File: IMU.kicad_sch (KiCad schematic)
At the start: 1 part, among them U1 RASPBERRY_PI_ZERO_2_W

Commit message: IMU schematic made
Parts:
- added J1: Conn_01x07_Socket, symbol Connector:Conn_01x07_Socket
- added J2: LCD Display, symbol Connector:Conn_01x04_Socket
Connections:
- net IMU_VCC: now reaches U1.1 (3V3_1)
- net IMU_VCC: now also J1.1 (Pin_1)
- net LCD_VCC: now reaches U1.17 (3V3_17)
- net LCD_VCC: now also J2.3 (Pin_3)
- net LCD_SDA: now reaches U1.24 (GPIO8/SPI_~{CE0})
- net LCD_SDA: now also J2.2 (Pin_2)
- net LCD_SCL: now reaches U1.26 (GPIO7/SPI_~{CE1})
- net LCD_SCL: now also J2.1 (Pin_1)
- net IMU_SCL: now reaches U1.29 (GPIO5)
- net IMU_SCL: now also J1.3 (Pin_3)
- net IMU_SDA: now reaches U1.31 (GPIO6)
- net IMU_SDA: now also J1.4 (Pin_4)
- net IMU_GND: now reaches U1.6 (GND_6)
- net IMU_GND: now also J1.2 (Pin_2)
- net LCD_GND: now reaches U1.9 (GND_9)
- net LCD_GND: now also J2.4 (Pin_4)
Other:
- note added: "IMU PINS: 1 - VCC 2 - GND 3 - SCL 4 - SDA 5 - XDA 6 - XCL 7 - INT"
- note added: "LCD PINS: 1 - SDA 2 - SCL 3 - VCC 4 - GND"
- moved on the sheet: U1

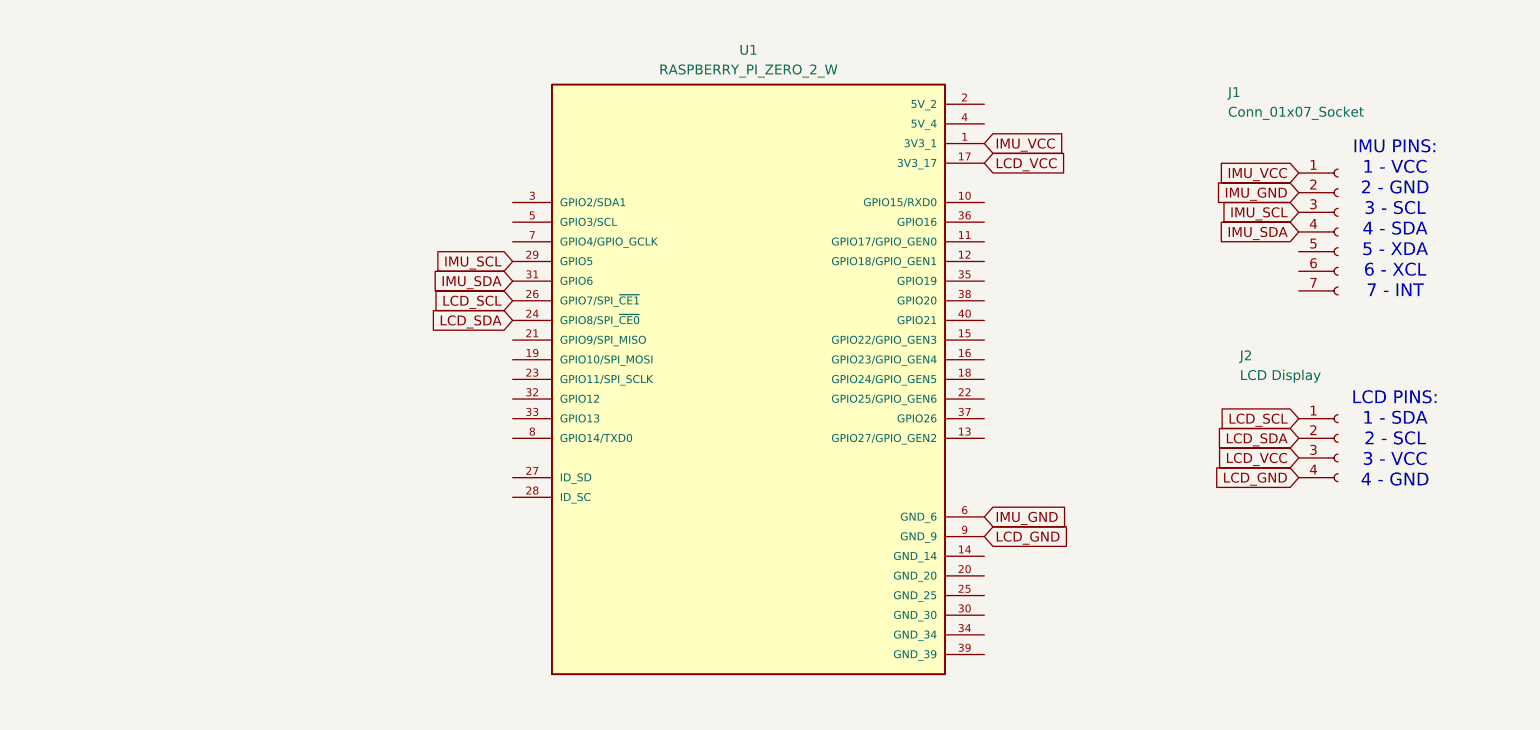
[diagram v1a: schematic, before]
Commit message: Adjusted schematic
Pullup resistors + decoupling capacitors
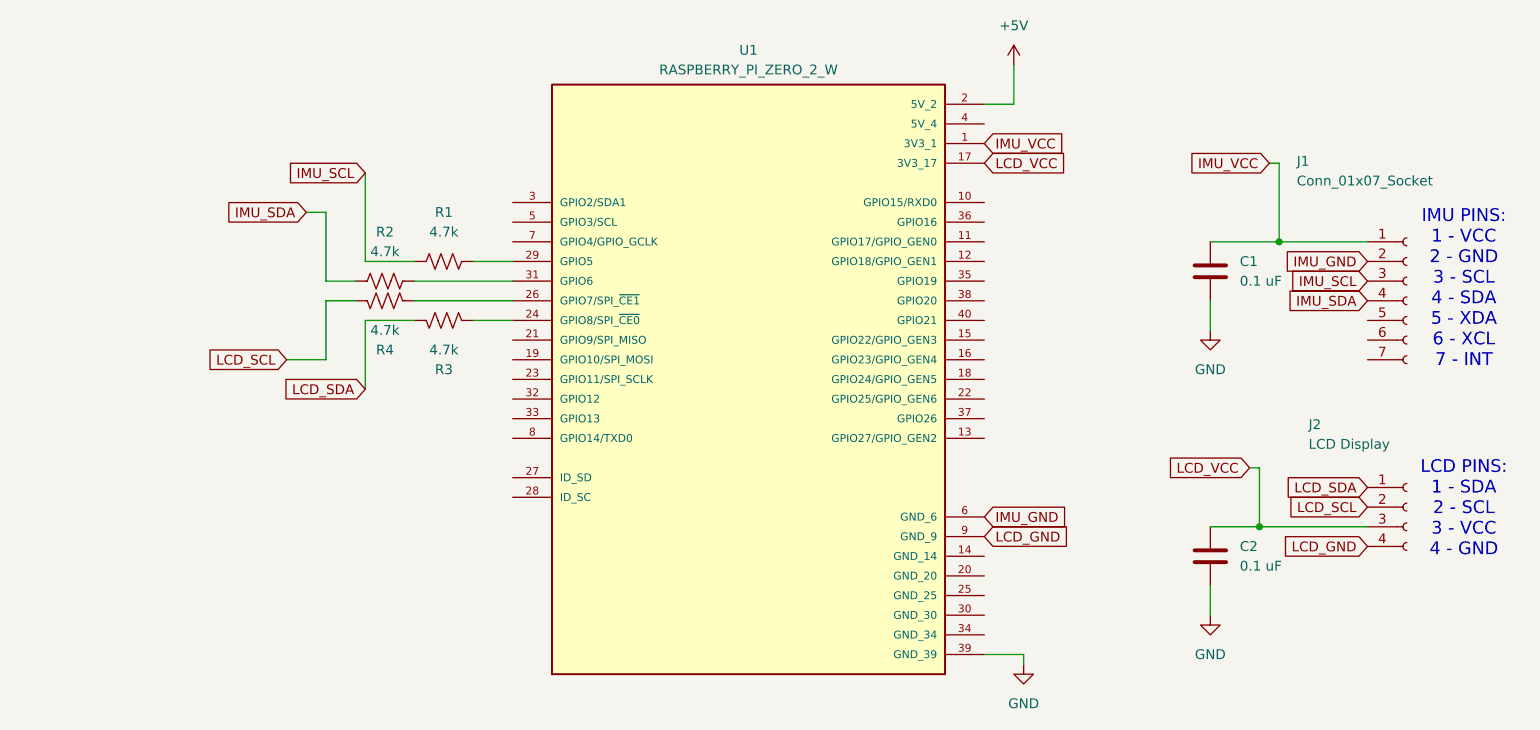
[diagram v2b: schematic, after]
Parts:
- added C1, C2: 0.1 uF, symbol Device:C
- added R1, R2, R3, R4: 4.7k, symbol Device:R_US
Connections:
- net IMU_SCL: now also R1.1; no longer U1.29 (GPIO5)
- net IMU_SDA: now also R2.1; no longer U1.31 (GPIO6)
- net IMU_VCC: now also C1.1
- net LCD_SCL: now also J2.2 (Pin_2), R4.1; no longer J2.1 (Pin_1), U1.26 (GPIO7/SPI_~{CE1})
- net LCD_SDA: now also J2.1 (Pin_1), R3.1; no longer J2.2 (Pin_2), U1.24 (GPIO8/SPI_~{CE0})
- net LCD_VCC: now also C2.1
- net +5V: now reaches U1.2 (5V_2)
- net GND: now reaches U1.39 (GND_39)
- net GND: now also C1.2, C2.2
- new net: R2.2, U1.31 (GPIO6)
- new net: R4.2, U1.26 (GPIO7/SPI_~{CE1})
- new net: R3.2, U1.24 (GPIO8/SPI_~{CE0})
- new net: R1.2, U1.29 (GPIO5)
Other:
- moved on the sheet: J1, J2

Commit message: KiCad ERC
Clean ERC test now
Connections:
- no-connect marks 0 -> 33

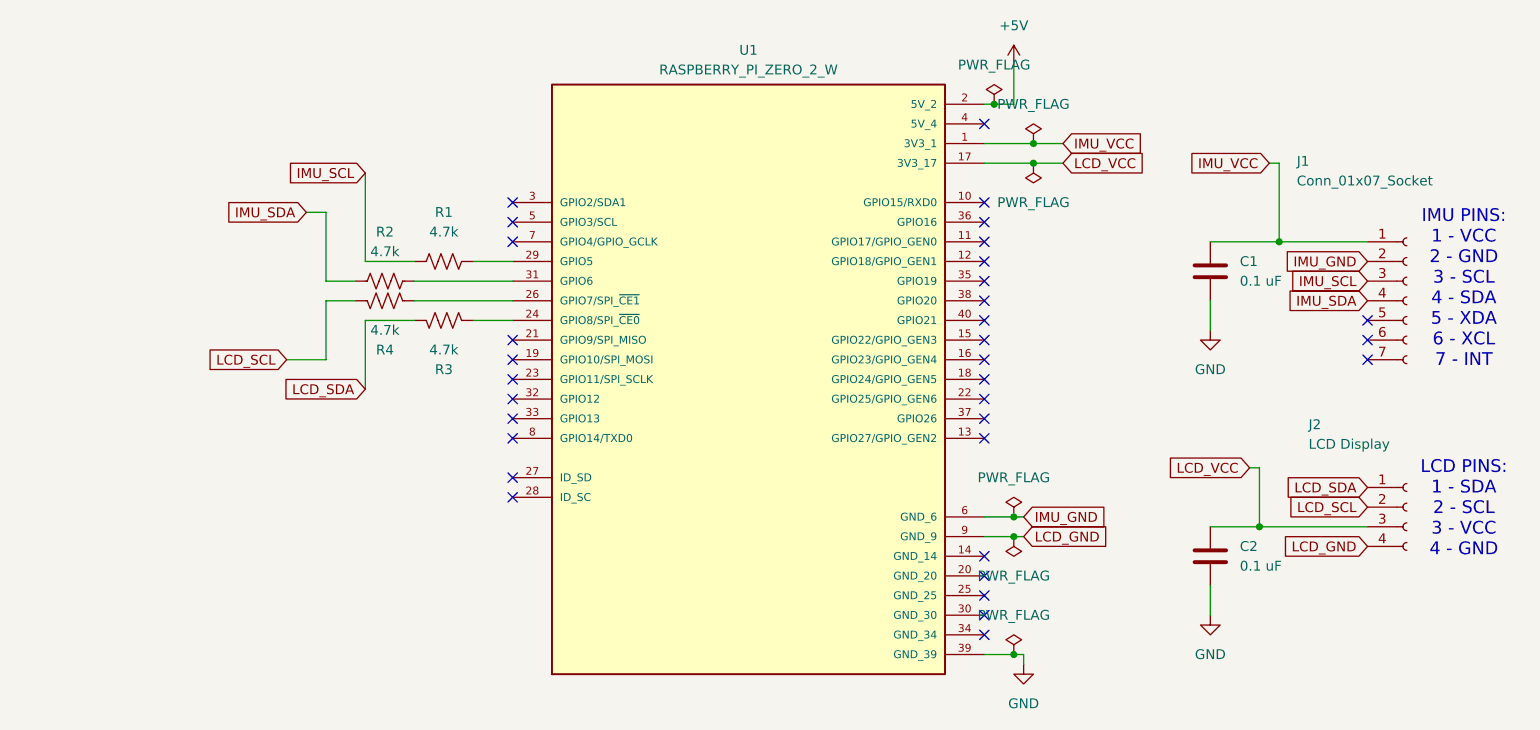
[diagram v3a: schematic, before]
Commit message: Schematic fixes
Fixed pullup resistors for SDL/SDA. Apparently needed for clean signals
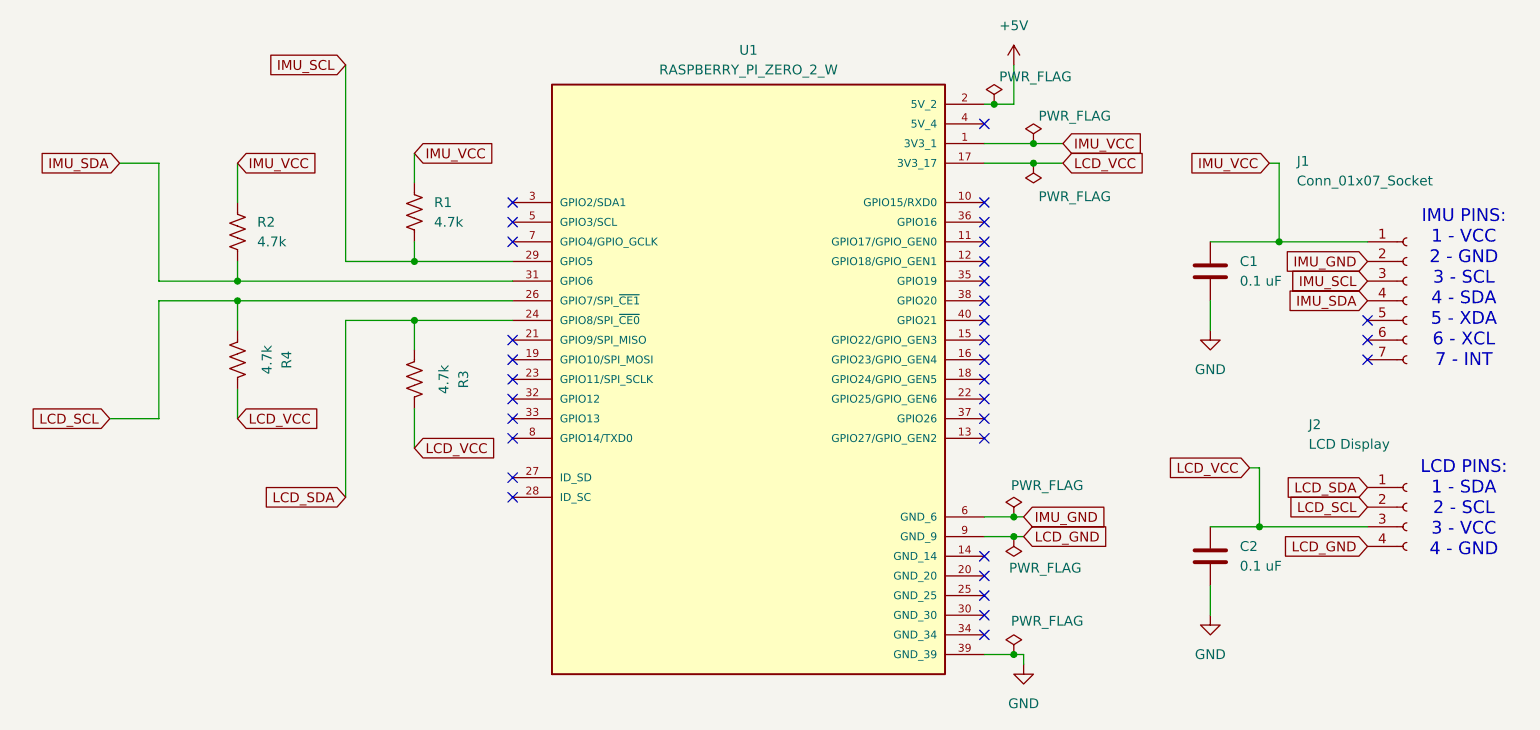
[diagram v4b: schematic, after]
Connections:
- net IMU_SCL: now also U1.29 (GPIO5)
- net IMU_SDA: now also U1.31 (GPIO6)
- net IMU_VCC: now also R1.2, R2.2
- net LCD_SCL: now also R4.2, U1.26 (GPIO7/SPI_~{CE1}); no longer R4.1
- net LCD_SDA: now also R3.2, U1.24 (GPIO8/SPI_~{CE0}); no longer R3.1
- net LCD_VCC: now also R3.1, R4.1
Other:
- moved on the sheet: R1, R2, R3, R4
